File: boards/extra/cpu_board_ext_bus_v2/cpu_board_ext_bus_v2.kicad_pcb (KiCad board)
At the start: 2 copper layers, 95.2 x 95.2 mm, 43 parts, among them J1 Exp. Conn. A, J2 Exp. Conn. B, J3 Power, J4 Exp. Conn. C, J5 EXT_CLK, J6 CPU_CLK_SEL, J7 BUS_CLK_SEL, U1 Z80CPPLC44, U2 GAL16V8, U3 74LS244, U4 74LS244, U5 74LS245, U6 74LS244, U7 74LS30, U8 ATF1502AS-7JX44, X1 INT_CLK

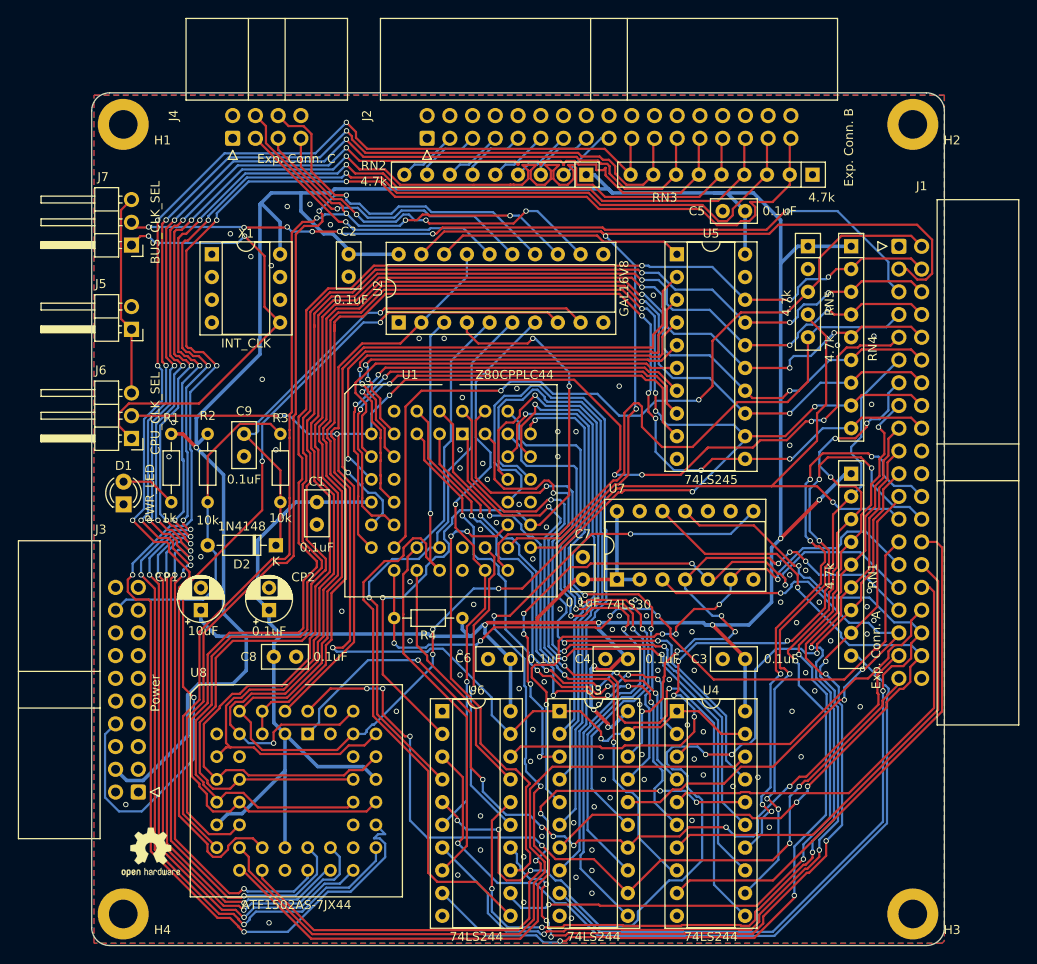
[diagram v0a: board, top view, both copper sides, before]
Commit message: Updated CPU board V2 with extension bus
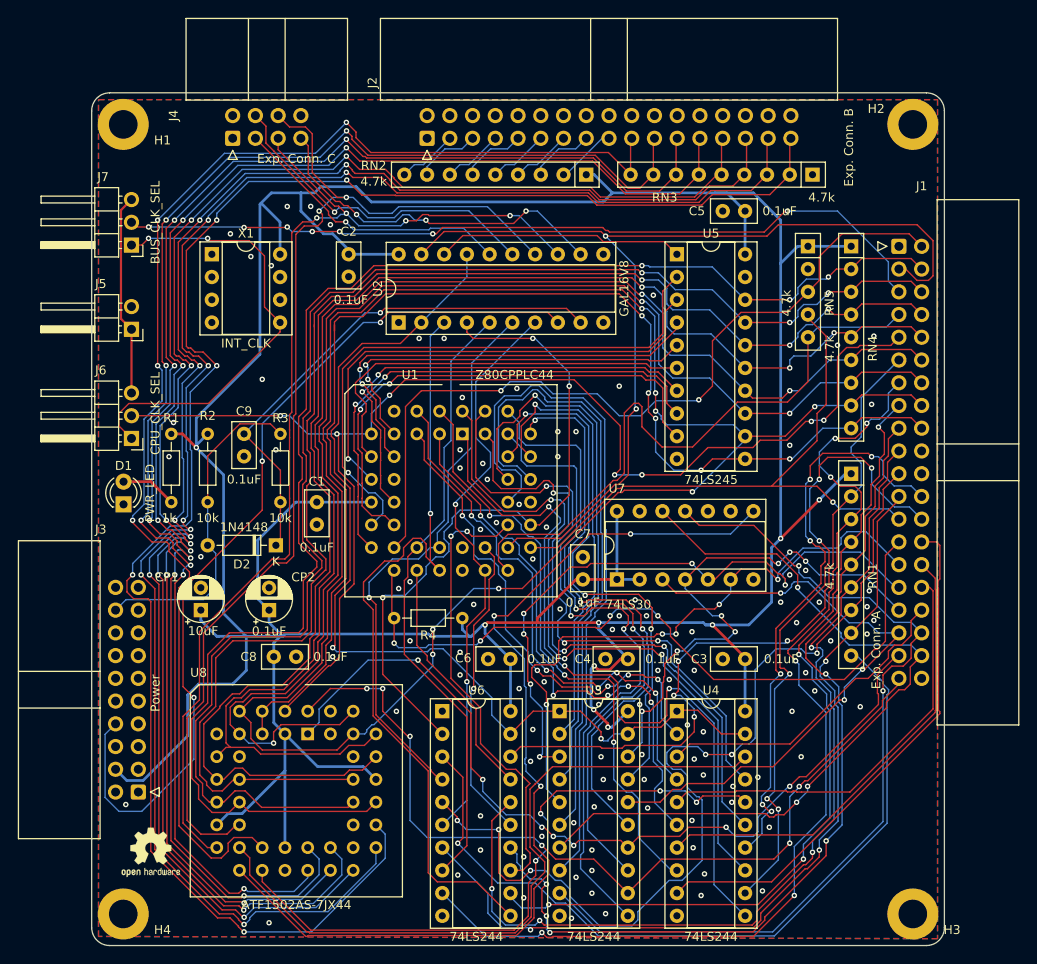
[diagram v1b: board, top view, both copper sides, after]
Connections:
- net Net-(D1-A) renamed /LED+
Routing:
- net /M_A17: track 191.5 -> 176.0 mm
- net /M_A14: track 197.5 -> 191.9 mm
- net /M_A18: track 171.1 -> 168.4 mm
- net /M_A15: track 185.8 -> 183.8 mm
- net /+5V: track 451.1 -> 452.2 mm
- net /~{B_WR}: track 102.9 -> 101.8 mm
- net /MCU/D5: track 50.6 -> 49.7 mm
- net /MCU/BUSACK: track 112.2 -> 111.4 mm
- net /M_A21: track 149.5 -> 150.3 mm
- net /MCU/D6: track 55.9 -> 55.1 mm
- net /Memory Mapper/~{MMU_CS}: track 109.0 -> 108.3 mm
- net /B_D6: track 159.7 -> 160.4 mm
- net /~{RESET0}: track 59.0 -> 58.4 mm
- net /~{B_RFSH}: track 97.3 -> 96.7 mm
- net /GND: vias 98 -> 106
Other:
- rule pad_to_mask_clearance: 0.2 -> 0
